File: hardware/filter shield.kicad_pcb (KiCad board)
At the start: 2 copper layers, 101.6 x 53.3 mm, 27 parts, among them J1 Screw_Terminal_01x03, J10 analog pins, J2 Screw_Terminal_01x03, J3 TR switch Connector, J4 5V distribution, J5 12V distribution, J6 Screw_Terminal_01x03, J7 Radioberry Connector, J8 BPF Connector, J9 LPF Connector, P10 CONN_01X01, P13 CONN_01X01, P8 CONN_01X01, Q1 PN2222A, Q2 PN2222A, Q3 PN2222A, Q4 PN2222A, Q5 PN2222A, Q6 PN2222A, U1 BOB-12009

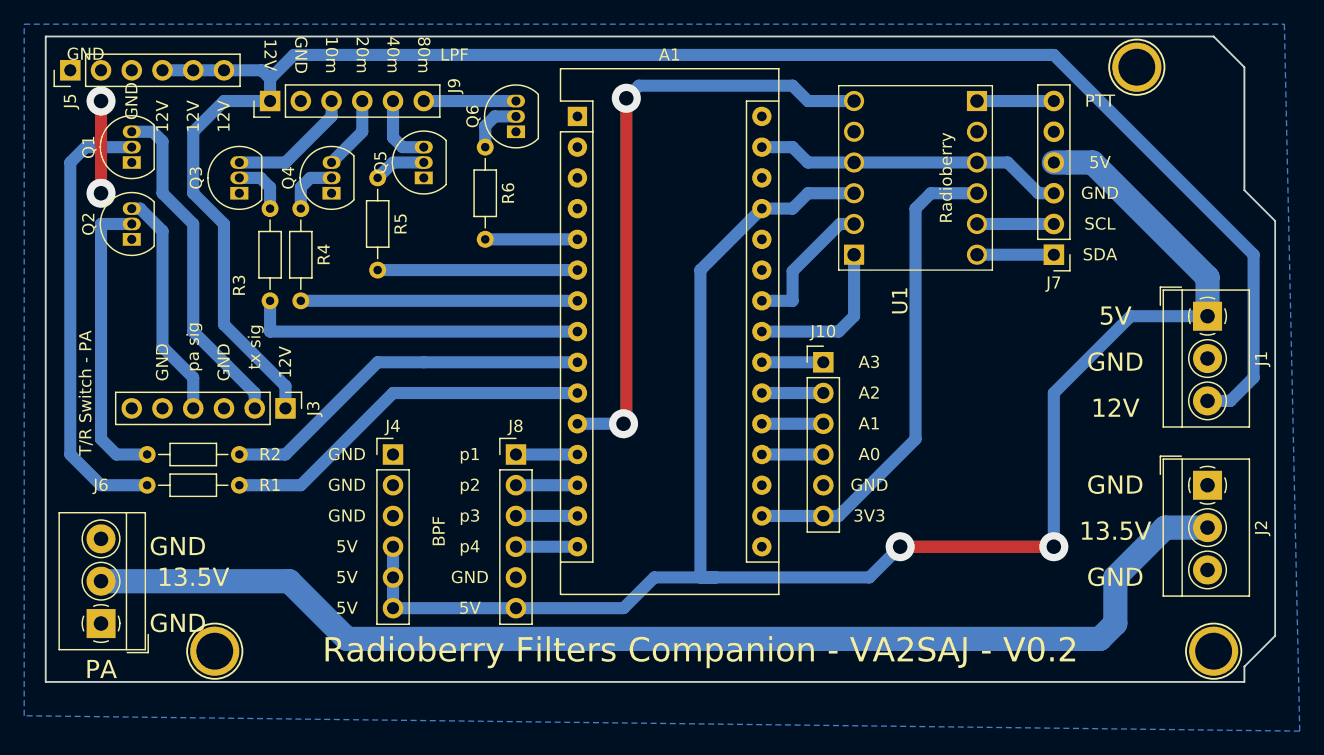
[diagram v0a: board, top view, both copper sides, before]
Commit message: Change screw terminal to 5mm footprint
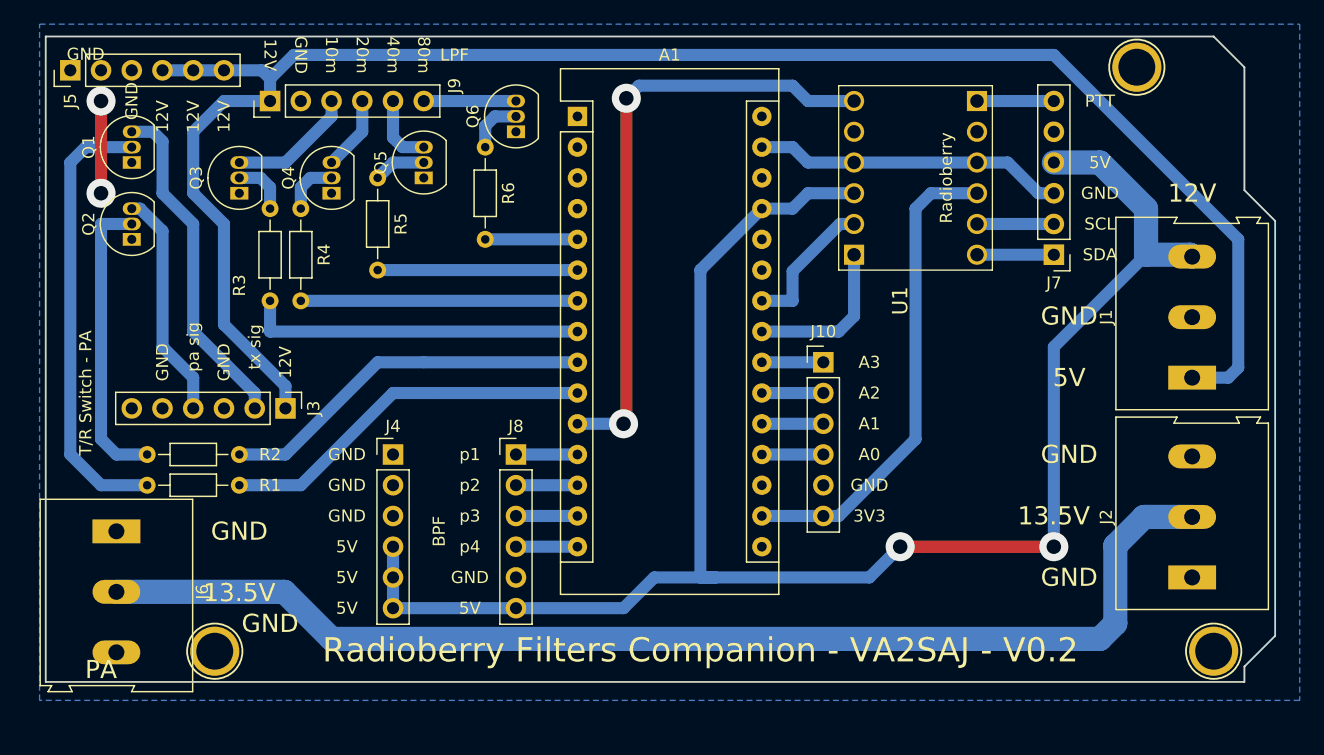
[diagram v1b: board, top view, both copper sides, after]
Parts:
- J1, J2, J6: footprint TerminalBlock_4Ucon:TerminalBlock_4Ucon_1x03_P3.50mm_Horizontal -> TerminalBlock:TerminalBlock_Altech_AK300-3_P5.00mm
- moved J6 7.73 mm to (109.2, 109.2), turned to 270 degrees
- moved J2 7.73 mm to (198.1, 113.0), turned to 90 degrees
- moved J1 5.24 mm to (198.1, 96.5), turned to 90 degrees
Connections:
- J1 pad 1: +5V -> +12V
- J1 pad 3: +12V -> +5V
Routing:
- net +5V: track 152.9 -> 149.2 mm
- net +12V: track 148.1 -> 146.3 mm
- net +15V: track 99.5 -> 98.5 mm
